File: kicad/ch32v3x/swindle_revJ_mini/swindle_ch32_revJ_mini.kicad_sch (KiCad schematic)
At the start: 22 parts, among them J2_DFU1 con2, Q1-A2SHB1 DMG2302U, U1 CH32V303RCT6, Y1 8Mhz

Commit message: Kicad update: ch32: update pcb , add boot pin control ch32: Ground PB2 so that the internal bootloader is on USB rp_zero_mini :add mostfet to rp zero mini
general update
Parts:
- added J3_BL1: con2, Connector_PinHeader_1.27mm:PinHeader_1x02_P1.27mm_Vertical, symbol Connector:Conn_01x02_Pin
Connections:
- net +3.3V: now also J3_BL1.1 (Pin_1)
- net GND: now also U1.28 (PB2)
- net at R11.1, U1.60 (BOOT0): now also J3_BL1.2 (Pin_2)

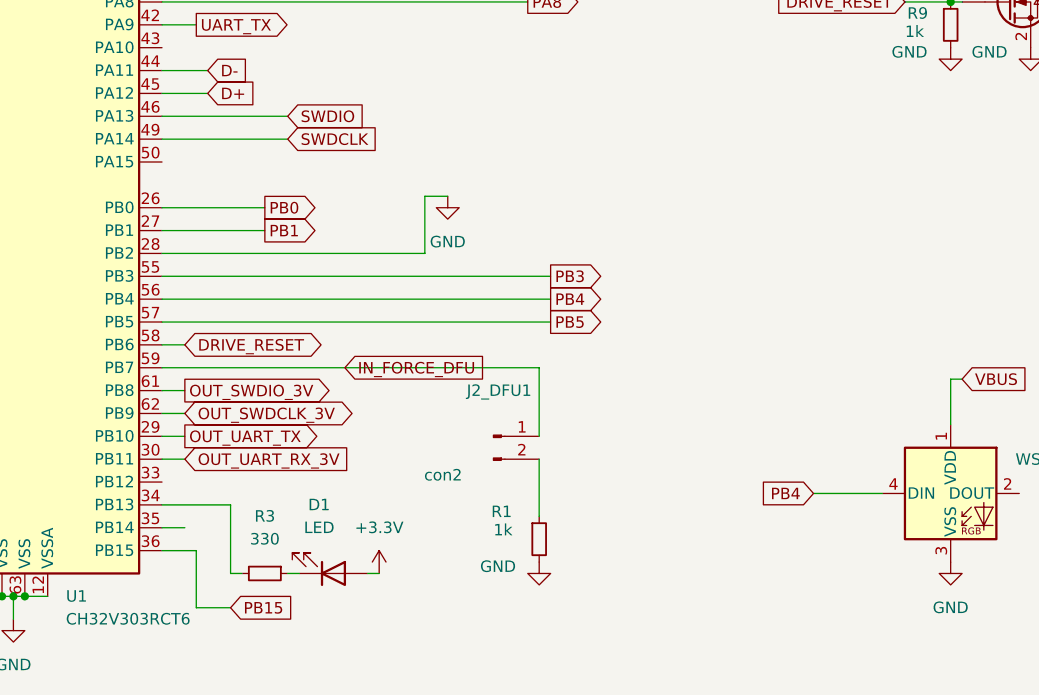
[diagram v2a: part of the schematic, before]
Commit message: kicad: update ch32 with the pullup
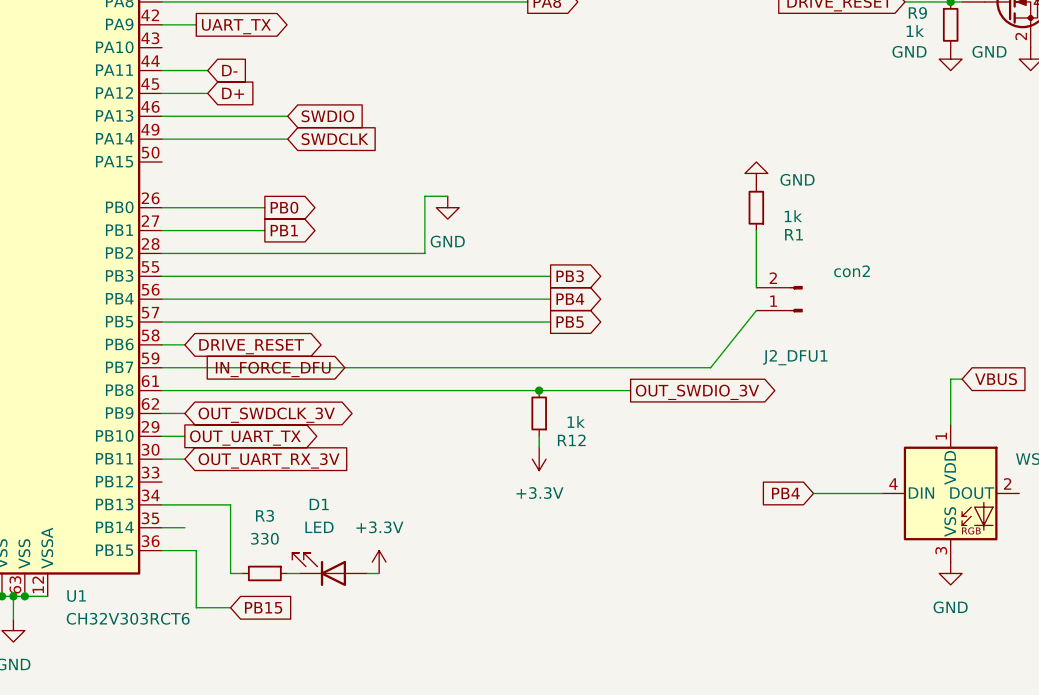
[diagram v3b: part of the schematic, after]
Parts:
- added R12: 1k, Resistor_SMD:R_0603_1608Metric, symbol Device:R_Small
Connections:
- net +3.3V: now also R12.1
- net OUT_SWDIO_3V: now also R12.2
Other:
- moved on the sheet: J2_DFU1, R1
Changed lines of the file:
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@@
 	)
 	(junction
+		(at 128.27 130.81)
+		(diameter 0)
+		(color 0 0 0 0)
+	)
+	(junction
 		(at 66.04 62.23)
 		(diameter 0)
@@
 	(wire
 		(pts
+			(xy 147.32 128.27) (xy 152.4 121.92)
+		)
+		(stroke
+			(width 0)
+			(type default)
+		)
+	)
+	(wire
+		(pts
 			(xy 105.41 29.21) (xy 109.22 29.21)
 		)
@@
 	(wire
 		(pts
+			(xy 128.27 130.81) (xy 138.43 130.81)
+		)
+		(stroke
+			(width 0)
+			(type default)
+		)
+	)
+	(wire
+		(pts
 			(xy 182.88 74.93) (xy 182.88 77.47)
 		)
@@
 	(wire
 		(pts
-			(xy 128.27 128.27) (xy 128.27 135.89)
+			(xy 86.36 128.27) (xy 147.32 128.27)
+		)
+		(stroke
+			(width 0)
+			(type default)
+		)
+	)
+	(wire
+		(pts
+			(xy 128.27 135.89) (xy 128.27 137.16)
 		)
 		(stroke
@@
 	(wire
 		(pts
-			(xy 128.27 138.43) (xy 128.27 144.78)
-		)
-		(stroke
-			(width 0)
-			(type default)
-		)
-	)
-	(wire
-		(pts
-			(xy 86.36 128.27) (xy 128.27 128.27)
+			(xy 152.4 119.38) (xy 152.4 113.03)
 		)
 		(stroke
@@
 	(wire
 		(pts
-			(xy 86.36 130.81) (xy 88.9 130.81)
+			(xy 86.36 130.81) (xy 128.27 130.81)
 		)
 		(stroke
@@
 	(global_label "OUT_SWDIO_3V"
 		(shape output)
-		(at 88.9 130.81 0)
+		(at 138.43 130.81 0)
 		(fields_autoplaced yes)
 		(effects
@@
 		)
 		(property "Intersheetrefs" "${INTERSHEET_REFS}"
-			(at 105.6133 130.81 0)
+			(at 155.1433 130.81 0)
 			(hide yes)
 			(show_name no)
@@
 	(global_label "IN_FORCE_DFU"
 		(shape input)
-		(at 106.68 128.27 0)
+		(at 106.68 128.27 180)
 		(fields_autoplaced yes)
 		(effects
@@
 				(size 1.27 1.27)
 			)
-			(justify left)
+			(justify right)
 		)
 		(property "Intersheetrefs" "${INTERSHEET_REFS}"
-			(at 123.3329 128.27 0)
+			(at 90.0271 128.27 0)
 			(hide yes)
 			(show_name no)
@@
 					(size 1.27 1.27)
 				)
-				(justify left)
+				(justify right)
 			)
 		)
@@
 	(symbol
 		(lib_id "Device:R_Small")
-		(at 128.27 147.32 0)
+		(at 152.4 110.49 180)
 		(unit 1)
 		(body_style 1)
@@
 		(dnp no)
 		(property "Reference" "R1"
-			(at 122.936 144.272 0)
+			(at 157.734 113.538 0)
 			(show_name no)
 			(do_not_autoplace no)
@@
 		)
 		(property "Value" "1k"
-			(at 123.19 146.304 0)
+			(at 157.48 111.506 0)
 			(show_name no)
 			(do_not_autoplace no)
@@
 		)
 		(property "Footprint" "Resistor_SMD:R_0603_1608Metric"
-			(at 128.27 147.32 0)
+			(at 152.4 110.49 0)
 			(hide yes)
 			(show_name no)
@@
 		)
 		(property "Datasheet" ""
-			(at 128.27 147.32 0)
+			(at 152.4 110.49 0)
 			(hide yes)
 			(show_name no)
@@
 		)
 		(property "Description" ""
-			(at 128.27 147.32 0)
+			(at 152.4 110.49 0)
 			(hide yes)
 			(show_name no)
@@
 	)
 	(symbol
+		(lib_id "power:+3.3V")
+		(at 128.27 137.16 0)
+		(mirror x)
+		(unit 1)
+		(body_style 1)
+		(exclude_from_sim no)
+		(in_bom yes)
+		(on_board yes)
+		(in_pos_files yes)
+		(dnp no)
+		(property "Reference" "#PWR027"
+			(at 128.27 133.35 0)
+			(hide yes)
+			(show_name no)
+			(do_not_autoplace no)
+			(effects
+				(font
+					(size 1.27 1.27)
+				)
+			)
+		)
+		(property "Value" "+3.3V"
+			(at 128.27 142.24 0)
+			(show_name no)
+			(do_not_autoplace no)
+			(effects
+				(font
+					(size 1.27 1.27)
+				)
+			)
+		)
+		(property "Footprint" ""
+			(at 128.27 137.16 0)
+			(hide yes)
+			(show_name no)
+			(do_not_autoplace no)
+			(effects
+				(font
+					(size 1.27 1.27)
+				)
+			)
+		)
+		(property "Datasheet" ""
+			(at 128.27 137.16 0)
+			(hide yes)
+			(show_name no)
+			(do_not_autoplace no)
+			(effects
+				(font
+					(size 1.27 1.27)
+				)
+			)
+		)
+		(property "Description" ""
+			(at 128.27 137.16 0)
+			(hide yes)
+			(show_name no)
+			(do_not_autoplace no)
+			(effects
+				(font
+					(size 1.27 1.27)
+				)
+			)
+		)
+		(pin "1"
+		)
+		(instances
+			(project "swindle_ch32_revJ_mini"
+				(path "/fbe443d6-6d74-4abc-9dee-16e0160553bc"
+					(reference "#PWR027")
+					(unit 1)
+				)
+			)
+		)
+	)
+	(symbol
 		(lib_id "Device:C_Small")
 		(at 105.41 26.67 0)
@@
 	)
 	(symbol
+		(lib_id "Device:R_Small")
+		(at 128.27 133.35 180)
+		(unit 1)
+		(body_style 1)
+		(exclude_from_sim no)
+		(in_bom yes)
+		(on_board yes)
+		(in_pos_files yes)
+		(dnp no)
+		(property "Reference" "R12"
+			(at 133.604 136.398 0)
+			(show_name no)
+			(do_not_autoplace no)
+			(effects
+				(font
+					(size 1.27 1.27)
+				)
+				(justify left)
+			)
+		)
+		(property "Value" "1k"
+			(at 133.35 134.366 0)
+			(show_name no)
+			(do_not_autoplace no)
+			(effects
+				(font
+					(size 1.27 1.27)
+				)
+				(justify left)
+			)
+		)
+		(property "Footprint" "Resistor_SMD:R_0603_1608Metric"
+			(at 128.27 133.35 0)
+			(hide yes)
+			(show_name no)
+			(do_not_autoplace no)
+			(effects
+				(font
+					(size 1.27 1.27)
+				)
+			)
+		)
+		(property "Datasheet" ""
+			(at 128.27 133.35 0)
+			(hide yes)
+			(show_name no)
+			(do_not_autoplace no)
+			(effects
+				(font
+					(size 1.27 1.27)
+				)
+			)
+		)
+		(property "Description" ""
+			(at 128.27 133.35 0)
+			(hide yes)
+			(show_name no)
+			(do_not_autoplace no)
+			(effects
+				(font
+					(size 1.27 1.27)
+				)
+			)
+		)
+		(pin "1"
+		)
+		(pin "2"
+		)
+		(instances
+			(project "swindle_ch32_revJ_mini"
+				(path "/fbe443d6-6d74-4abc-9dee-16e0160553bc"
+					(reference "R12")
+					(unit 1)
+				)
+			)
+		)
+	)
+	(symbol
 		(lib_id "power:+3.3V")
 		(at 30.48 72.39 0)
@@
 	(symbol
 		(lib_id "Connector:Conn_01x02_Pin")
-		(at 123.19 135.89 0)
+		(at 157.48 121.92 180)
 		(unit 1)
 		(body_style 1)
@@
 		(dnp no)
 		(property "Reference" "J2_DFU1"
-			(at 123.825 130.81 0)
+			(at 156.845 127 0)
 			(show_name no)
 			(do_not_autoplace no)
@@
 		)
 		(property "Value" "con2"
-			(at 117.602 140.208 0)
+			(at 163.068 117.602 0)
 			(show_name no)
 			(do_not_autoplace no)
@@
 		)
 		(property "Footprint" "Connector_PinHeader_1.27mm:PinHeader_1x02_P1.27mm_Vertical"
-			(at 123.19 135.89 0)
+			(at 157.48 121.92 0)
 			(hide yes)
 			(show_name no)
@@
 		)
 		(property "Datasheet" ""
-			(at 123.19 135.89 0)
+			(at 157.48 121.92 0)
 			(hide yes)
 			(show_name no)
@@
 		)
 		(property "Description" "Generic connector, single row, 01x02, script generated"
-			(at 123.19 135.89 0)
+			(at 157.48 121.92 0)
 			(hide yes)
 			(show_name no)
@@
 	(symbol
 		(lib_id "power:GND")
-		(at 128.27 149.86 0)
+		(at 152.4 107.95 180)
 		(unit 1)
 		(body_style 1)
@@
 		(dnp no)
 		(property "Reference" "#PWR018"
-			(at 128.27 156.21 0)
+			(at 152.4 101.6 0)
 			(hide yes)
 			(show_name no)
@@
 		)
 		(property "Value" "GND"
-			(at 123.698 150.368 0)
+			(at 156.972 107.442 0)
 			(show_name no)
 			(do_not_autoplace no)
@@
 		)
 		(property "Footprint" ""
-			(at 128.27 149.86 0)
+			(at 152.4 107.95 0)
 			(hide yes)
 			(show_name no)
@@
 		)
 		(property "Datasheet" ""
-			(at 128.27 149.86 0)
+			(at 152.4 107.95 0)
 			(hide yes)
 			(show_name no)
@@
 		)
 		(property "Description" ""
-			(at 128.27 149.86 0)
+			(at 152.4 107.95 0)
 			(hide yes)
 			(show_name no)
